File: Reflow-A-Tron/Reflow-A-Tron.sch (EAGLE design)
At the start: 14 parts, among them IC1 ATMEGA644-10PU, Q1 FOXSLF/200-20, U2 MC7805, U4 MAX6675

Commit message: more reflow controller work
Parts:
- added C10: 4.7uF, neilbetham:SMD-CAP-0805
- added C3, C4: 100nF, neilbetham:SMD-CAP-0805
- added J1: (no value), neilbetham:XM7D-0512
- added JP1: AVR_SPI_PRG_6NS, SparkFun-Connectors:AVR_SPI_PRG_6NS
- added POWER: (no value), SparkFun-Connectors:M025MM
- added R3, R4: 27, resistor:R-US_M0805
- added THERMOCOUPLE: (no value), SparkFun-Connectors:M023.5MM
- added U1: (no value), neilbetham:FT230X
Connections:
- new net DM: R4.1, U1.USBDM
- new net DP: R3.1, U1.USBDP
- new net ID: J1.ID
- new net MOSI: IC1.PCINT13/MOSI_PB5, JP1.4
- new net N$3: J1.DM, R4.2
- new net N$4: J1.DP, R3.2
- new net USB-VCC: C10.2, C4.2, J1.VCC, U1.VCC
- new net VCCIO: C3.2, U1.3V3OUT, U1.VCCIO
- net 5V: now also JP1.2
- net GND: now also C10.1, C3.1, C4.1, J1.GND, JP1.6, POWER.2, U1.AGND, U1.GND
- net MISO: now also JP1.1
- net RESET: now also JP1.5
- net SCK: now also JP1.3
- net T+: now also THERMOCOUPLE.1
- net T-: now also THERMOCOUPLE.2
- net VCC: now also POWER.1

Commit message: JTAG programming
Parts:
- removed JP1: AVR_SPI_PRG_6NS, SparkFun-Connectors:AVR_SPI_PRG_6NS
- added D1: Green, SparkFun-LED:LED1206
- added D2: Blue, SparkFun-LED:LED1206
- added JP2: (no value), SparkFun-Connectors:M05X2PTH
- added R5: 150, resistor:R-US_R0805
- added R6: 85, resistor:R-US_R0805
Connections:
- new net N$10: IC1.PCINT25/TXD0_PD1, U1.RXD
- new net N$5: D1.A, R5.1
- new net N$6: D2.A, R6.1
- new net N$7: D2.C, U1.CBUS1
- new net N$8: D1.C, U1.CBUS2
- new net N$9: IC1.PCINT24/RXD0_PD0, U1.TXD
- new net TCK: IC1.PCINT18/TCK_PC2, JP2.1
- new net TDI: IC1.PCINT21/TDI_PC5, JP2.9
- new net TDO: IC1.PCINT20/TDO_PC4, JP2.3
- new net TMS: IC1.PCINT19/TMS_PC3, JP2.5
- net 5V: now also JP2.4, R5.2, R6.2, U1.VCC; no longer JP1.2
- net GND: now also JP2.10, JP2.2; no longer JP1.6
- net MISO: no longer JP1.1
- net MOSI: no longer JP1.4
- net RESET: now also JP2.6; no longer JP1.5
- net SCK: no longer JP1.3
- net USB-VCC: no longer U1.VCC
- net VCCIO: now also U1.RESET

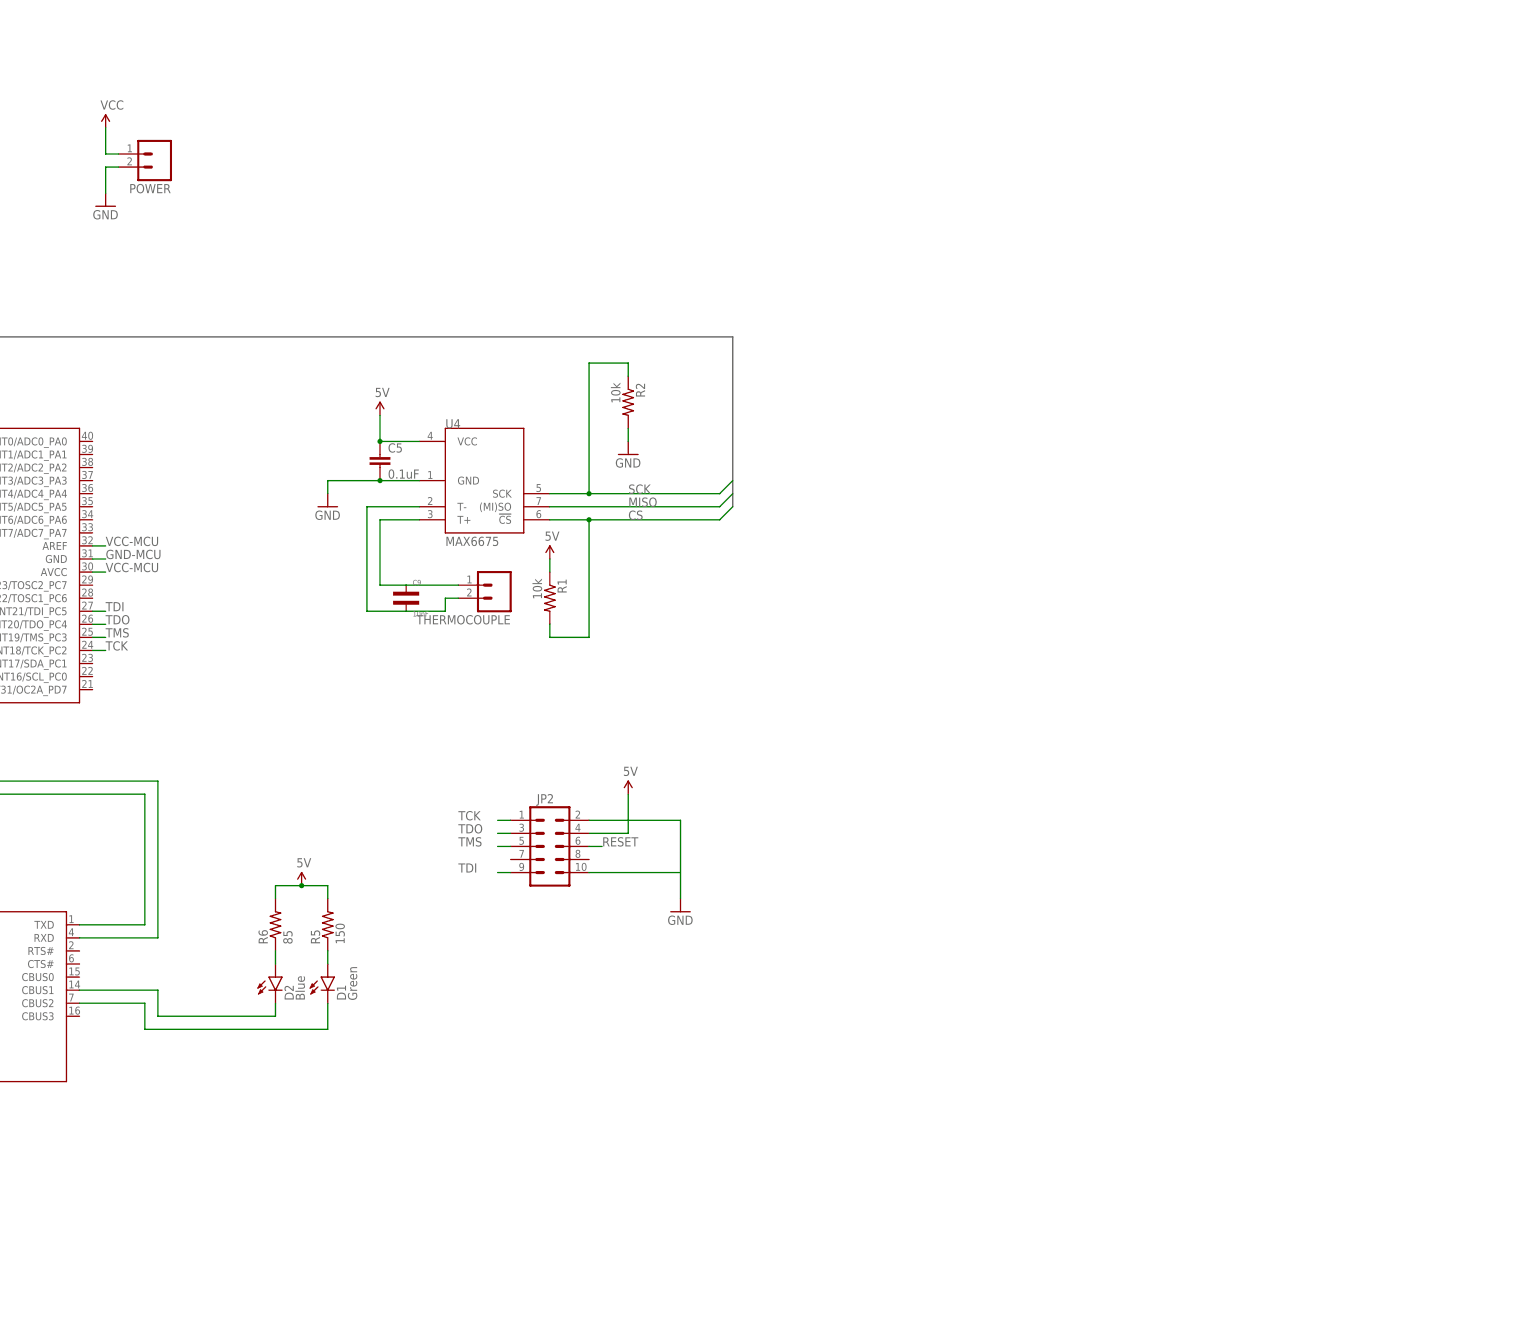
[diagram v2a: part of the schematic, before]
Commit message: triac connected
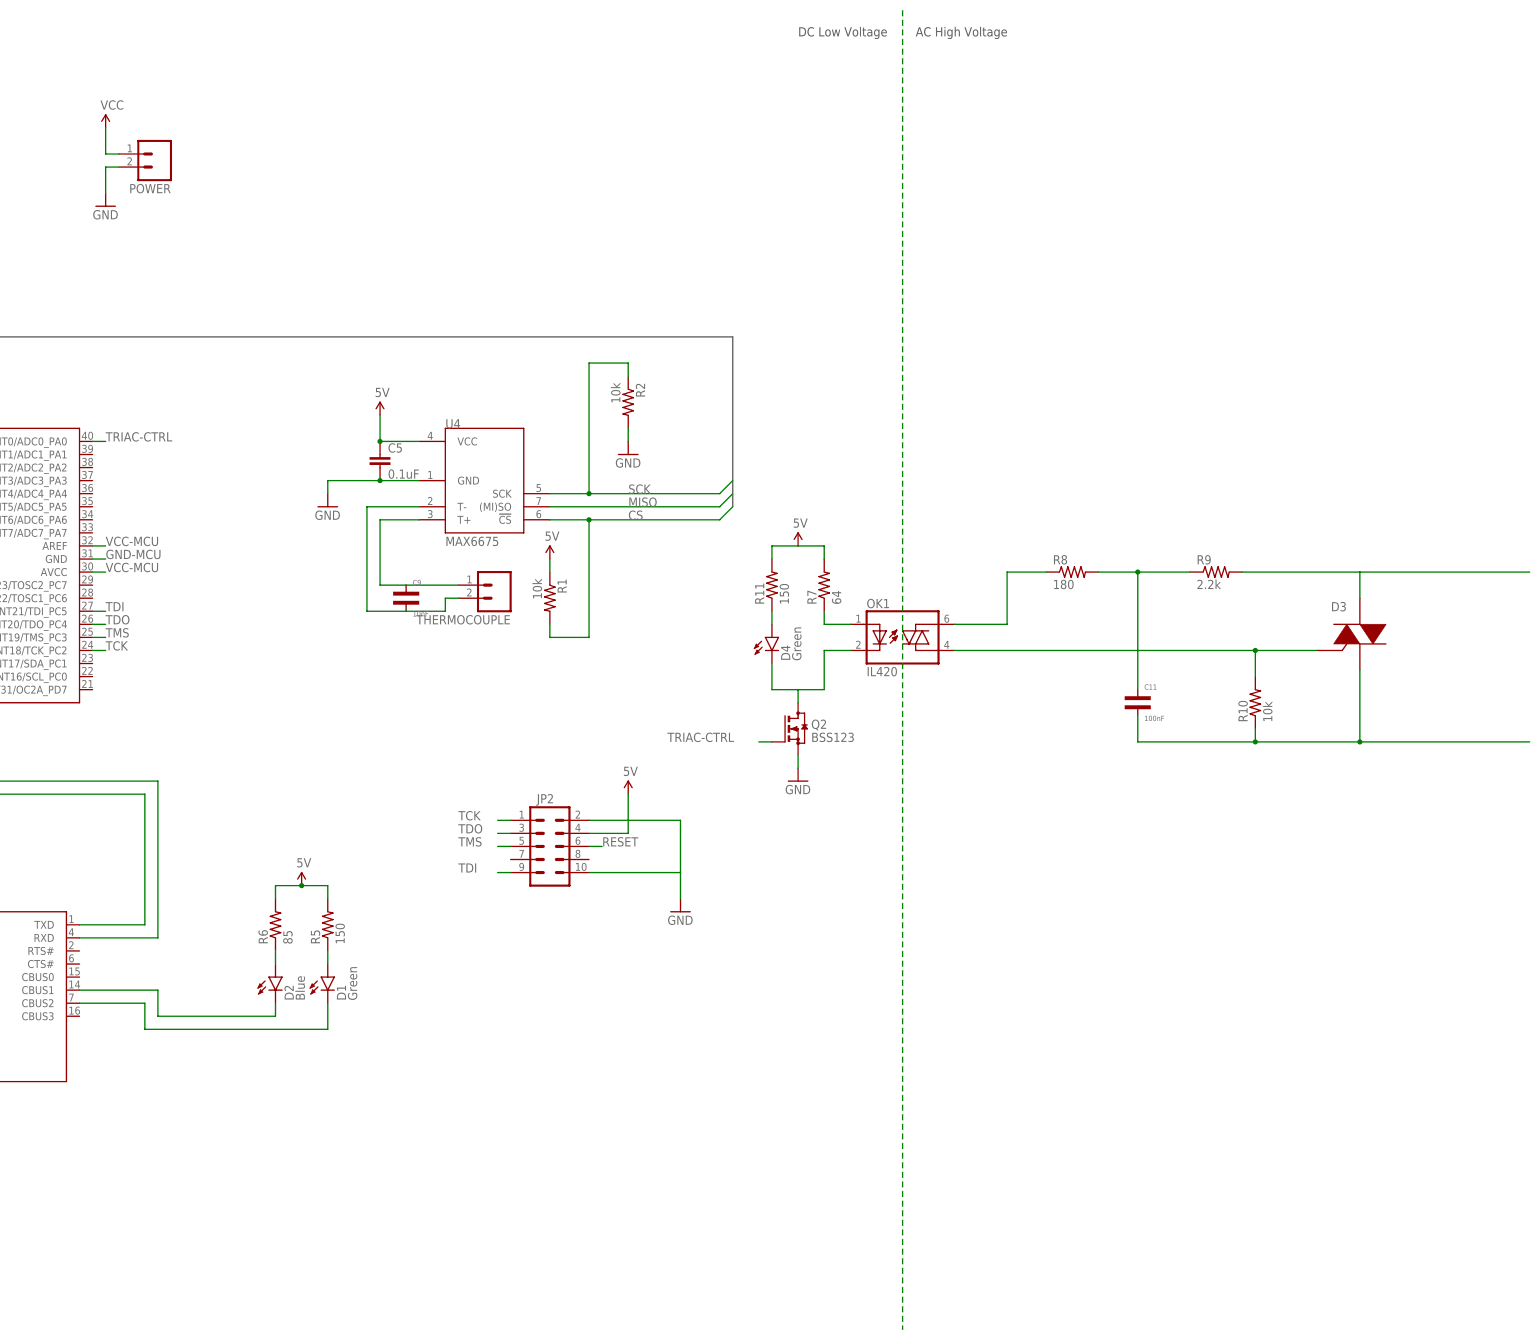
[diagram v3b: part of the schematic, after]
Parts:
- added C11: 100nF, neilbetham:SMD-CAP-0805
- added D3: (no value), neilbetham:T1250H
- added D4: Green, SparkFun-LED:LED1206
- added OK1: IL420, optocoupler:IL420
- added Q2: BSS123, transistor-small-signal:BSS123
- added R10: 10k, resistor:R-US_R0805
- added R11: 150, resistor:R-US_R0805
- added R7: 64, resistor:R-US_R0805
- added R8: 180, resistor:R-US_R0805
- added R9: 2.2k, resistor:R-US_R0805
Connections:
- new net N$12: OK1.A2, R8.1
- new net N$13: OK1.A, R7.1
- new net N$14: D3.G, OK1.A1, R10.2
- new net N$15: C11.2, R8.2, R9.1
- new net N$16: D3.A2, R9.2
- new net N$17: C11.1, D3.A1, R10.1
- new net N$18: R11.2, R7.2
- new net N$19: OK1.C
- new net N$20: D4.A, R11.1
- new net N$21: D4.C, Q2.D
- new net TRIAC-CTRL: IC1.PCINT0/ADC0_PA0, Q2.G
- net GND: now also Q2.S
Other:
- note added: "AC High Voltage"
- note added: "DC Low Voltage"
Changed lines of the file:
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@@
 <part name="GND6" library="SparkFun-Aesthetics" deviceset="GND" device=""/>
 <part name="SUPPLY5" library="SparkFun-Aesthetics" deviceset="5V" device=""/>
+<part name="D3" library="neilbetham" deviceset="T1250H" device=""/>
+<part name="OK1" library="optocoupler" deviceset="IL420" device=""/>
+<part name="GND9" library="SparkFun-Aesthetics" deviceset="GND" device=""/>
+<part name="R8" library="resistor" deviceset="R-US_" device="R0805" value="180"/>
+<part name="R9" library="resistor" deviceset="R-US_" device="R0805" value="2.2k"/>
+<part name="R10" library="resistor" deviceset="R-US_" device="R0805" value="10k"/>
+<part name="C11" library="neilbetham" deviceset="SMD-CAP" device="-0805" value="100nF"/>
+<part name="R7" library="resistor" deviceset="R-US_" device="R0805" value="64"/>
+<part name="SUPPLY10" library="SparkFun-Aesthetics" deviceset="5V" device=""/>
+<part name="D4" library="SparkFun-LED" deviceset="LED" device="1206" value="Green"/>
+<part name="R11" library="resistor" deviceset="R-US_" device="R0805" value="150"/>
+<part name="Q2" library="transistor-small-signal" deviceset="BSS123" device=""/>
 </parts>
 <sheets>
 <sheet>
 <plain>
+<text x="198.12" y="152.4" size="1.778" layer="97">DC Low Voltage</text>
+<text x="220.98" y="152.4" size="1.778" layer="97">AC High Voltage</text>
 </plain>
 <instances>
@@
 <instance part="GND6" gate="1" x="175.26" y="-17.78"/>
 <instance part="SUPPLY5" gate="G$1" x="165.1" y="5.08"/>
+<instance part="D3" gate="G$1" x="307.34" y="35.56" rot="MR0"/>
+<instance part="OK1" gate="G$1" x="218.44" y="35.56"/>
+<instance part="GND9" gate="1" x="198.12" y="7.62"/>
+<instance part="R8" gate="G$1" x="251.46" y="48.26"/>
+<instance part="R9" gate="G$1" x="279.4" y="48.26"/>
+<instance part="R10" gate="G$1" x="287.02" y="22.86" rot="R90"/>
+<instance part="C11" gate="G$1" x="264.16" y="22.86"/>
+<instance part="R7" gate="G$1" x="203.2" y="45.72" rot="R90"/>
+<instance part="SUPPLY10" gate="G$1" x="198.12" y="53.34"/>
+<instance part="D4" gate="G$1" x="193.04" y="35.56"/>
+<instance part="R11" gate="G$1" x="193.04" y="45.72" rot="R90"/>
+<instance part="Q2" gate="G$1" x="198.12" y="17.78"/>
 </instances>
 <busses>
@@
 <wire x1="157.48" y1="-10.16" x2="175.26" y2="-10.16" width="0.1524" layer="91"/>
 </segment>
+<segment>
+<pinref part="Q2" gate="G$1" pin="S"/>
+<pinref part="GND9" gate="1" pin="GND"/>
+<wire x1="198.12" y1="12.7" x2="198.12" y2="10.16" width="0.1524" layer="91"/>
+</segment>
 </net>
 <net name="RESET" class="0">
@@
 </segment>
 </net>
+<net name="N$11" class="0">
+<segment>
+<wire x1="218.44" y1="157.48" x2="218.44" y2="-99.06" width="0.1524" layer="91" style="shortdash"/>
+</segment>
+</net>
+<net name="N$13" class="0">
+<segment>
+<pinref part="OK1" gate="G$1" pin="A"/>
+<wire x1="203.2" y1="38.1" x2="208.28" y2="38.1" width="0.1524" layer="91"/>
+<wire x1="203.2" y1="38.1" x2="203.2" y2="40.64" width="0.1524" layer="91"/>
+<pinref part="R7" gate="G$1" pin="1"/>
+</segment>
+</net>
+<net name="N$12" class="0">
+<segment>
+<pinref part="R8" gate="G$1" pin="1"/>
+<wire x1="246.38" y1="48.26" x2="238.76" y2="48.26" width="0.1524" layer="91"/>
+<wire x1="238.76" y1="48.26" x2="238.76" y2="38.1" width="0.1524" layer="91"/>
+<pinref part="OK1" gate="G$1" pin="A2"/>
+<wire x1="238.76" y1="38.1" x2="228.6" y2="38.1" width="0.1524" layer="91"/>
+</segment>
+</net>
+<net name="N$14" class="0">
+<segment>
+<pinref part="OK1" gate="G$1" pin="A1"/>
+<wire x1="228.6" y1="33.02" x2="287.02" y2="33.02" width="0.1524" layer="91"/>
+<pinref part="D3" gate="G$1" pin="G"/>
+<pinref part="R10" gate="G$1" pin="2"/>
+<wire x1="287.02" y1="33.02" x2="298.831" y2="33.02" width="0.1524" layer="91"/>
+<wire x1="287.02" y1="27.94" x2="287.02" y2="33.02" width="0.1524" layer="91"/>
+<junction x="287.02" y="33.02"/>
+</segment>
+</net>
+<net name="N$15" class="0">
+<segment>
+<pinref part="R8" gate="G$1" pin="2"/>
+<pinref part="R9" gate="G$1" pin="1"/>
+<wire x1="256.54" y1="48.26" x2="264.16" y2="48.26" width="0.1524" layer="91"/>
+<pinref part="C11" gate="G$1" pin="2"/>
+<wire x1="264.16" y1="48.26" x2="274.32" y2="48.26" width="0.1524" layer="91"/>
+<wire x1="264.16" y1="25.4" x2="264.16" y2="48.26" width="0.1524" layer="91"/>
+<junction x="264.16" y="48.26"/>
+</segment>
+</net>
+<net name="N$16" class="0">
+<segment>
+<pinref part="R9" gate="G$1" pin="2"/>
+<wire x1="284.48" y1="48.26" x2="307.34" y2="48.26" width="0.1524" layer="91"/>
+<pinref part="D3" gate="G$1" pin="A2"/>
+<wire x1="307.34" y1="48.26" x2="340.36" y2="48.26" width="0.1524" layer="91"/>
+<wire x1="307.34" y1="43.18" x2="307.34" y2="48.26" width="0.1524" layer="91"/>
+</segment>
+</net>
+<net name="N$17" class="0">
+<segment>
+<pinref part="C11" gate="G$1" pin="1"/>
+<wire x1="264.16" y1="20.32" x2="264.16" y2="15.24" width="0.1524" layer="91"/>
+<wire x1="264.16" y1="15.24" x2="287.02" y2="15.24" width="0.1524" layer="91"/>
+<pinref part="R10" gate="G$1" pin="1"/>
+<wire x1="287.02" y1="15.24" x2="307.34" y2="15.24" width="0.1524" layer="91"/>
+<wire x1="307.34" y1="15.24" x2="340.36" y2="15.24" width="0.1524" layer="91"/>
+<wire x1="287.02" y1="17.78" x2="287.02" y2="15.24" width="0.1524" layer="91"/>
+<pinref part="D3" gate="G$1" pin="A1"/>
+<wire x1="307.34" y1="29.21" x2="307.34" y2="15.24" width="0.1524" layer="91"/>
+<junction x="287.02" y="15.24"/>
+<junction x="307.34" y="15.24"/>
+</segment>
+</net>
+<net name="TRIAC-CTRL" class="0">
+<segment>
+<pinref part="IC1" gate="G$1" pin="PCINT0/ADC0_PA0"/>
+<wire x1="60.96" y1="73.66" x2="63.5" y2="73.66" width="0.1524" layer="91"/>
+<label x="63.5" y="73.66" size="1.778" layer="95"/>
+</segment>
+<segment>
+<pinref part="Q2" gate="G$1" pin="G"/>
+<wire x1="193.04" y1="15.24" x2="190.5" y2="15.24" width="0.1524" layer="91"/>
+<label x="172.72" y="15.24" size="1.778" layer="95"/>
+</segment>
+</net>
+<net name="N$18" class="0">
+<segment>
+<pinref part="SUPPLY10" gate="G$1" pin="5V"/>
+<pinref part="R11" gate="G$1" pin="2"/>
+<wire x1="198.12" y1="53.34" x2="193.04" y2="53.34" width="0.1524" layer="91"/>
+<wire x1="193.04" y1="53.34" x2="193.04" y2="50.8" width="0.1524" layer="91"/>
+<pinref part="R7" gate="G$1" pin="2"/>
+<wire x1="198.12" y1="53.34" x2="203.2" y2="53.34" width="0.1524" layer="91"/>
+<wire x1="203.2" y1="53.34" x2="203.2" y2="50.8" width="0.1524" layer="91"/>
+</segment>
+</net>
+<net name="N$20" class="0">
+<segment>
+<pinref part="R11" gate="G$1" pin="1"/>
+<pinref part="D4" gate="G$1" pin="A"/>
+<wire x1="193.04" y1="40.64" x2="193.04" y2="38.1" width="0.1524" layer="91"/>
+</segment>
+</net>
+<net name="N$19" class="0">
+<segment>
+<pinref part="OK1" gate="G$1" pin="C"/>
+<wire x1="208.28" y1="33.02" x2="203.2" y2="33.02" width="0.1524" layer="91"/>
+<wire x1="203.2" y1="25.4" x2="203.2" y2="33.02" width="0.1524" layer="91"/>
+</segment>
+</net>
+<net name="N$21" class="0">
+<segment>
+<pinref part="D4" gate="G$1" pin="C"/>
+<wire x1="193.04" y1="30.48" x2="193.04" y2="25.4" width="0.1524" layer="91"/>
+<wire x1="193.04" y1="25.4" x2="198.12" y2="25.4" width="0.1524" layer="91"/>
+<pinref part="Q2" gate="G$1" pin="D"/>
+<wire x1="198.12" y1="25.4" x2="203.2" y2="25.4" width="0.1524" layer="91"/>
+<wire x1="198.12" y1="25.4" x2="198.12" y2="22.86" width="0.1524" layer="91"/>
+</segment>
+</net>
